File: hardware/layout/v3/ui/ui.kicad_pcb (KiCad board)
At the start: 4 copper layers, 13.8 x 40.5 mm, 25 parts, among them J1 Carrier, J2 OLED, SW1 PRG/RST, SW2 FUNC, U1 74AHCT1G125

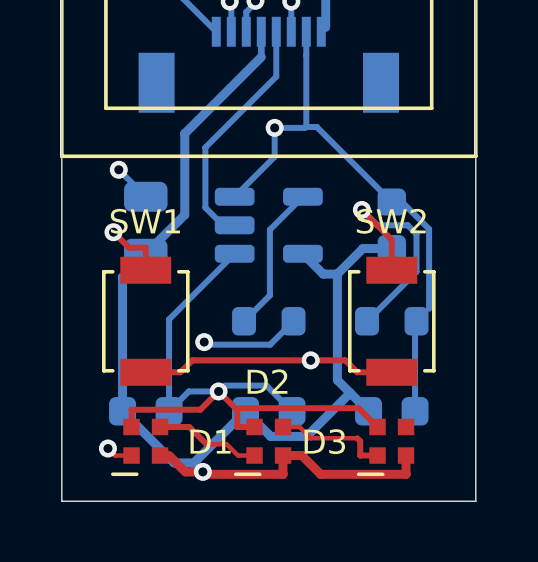
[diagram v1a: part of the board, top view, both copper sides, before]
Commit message: Added zero-length track segments to fix hairline joints where track ends grazed pads instead of fully entering them
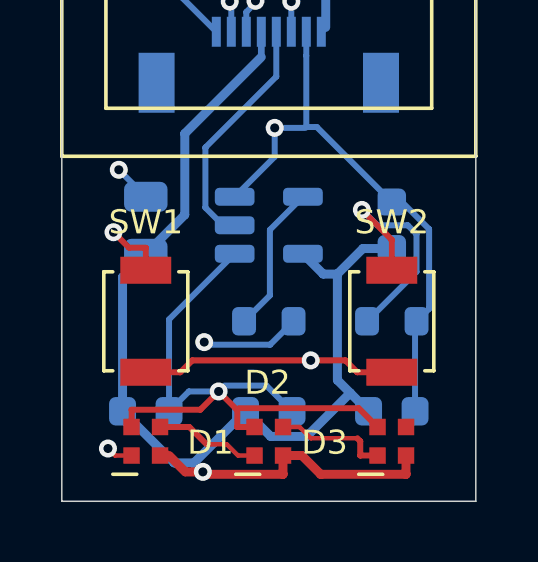
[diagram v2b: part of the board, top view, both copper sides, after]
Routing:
- net GND: track 74.0 -> 74.6 mm
